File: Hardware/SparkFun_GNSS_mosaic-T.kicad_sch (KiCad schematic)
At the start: 52 parts, among them J2 microSD, SW1 DPDT_Slide_SMD_7.2x3.5mm, SW2 SMD_5.2x5.2mm_h2.5mm, U1 mosaic-T, U4 74LVC2T45DC

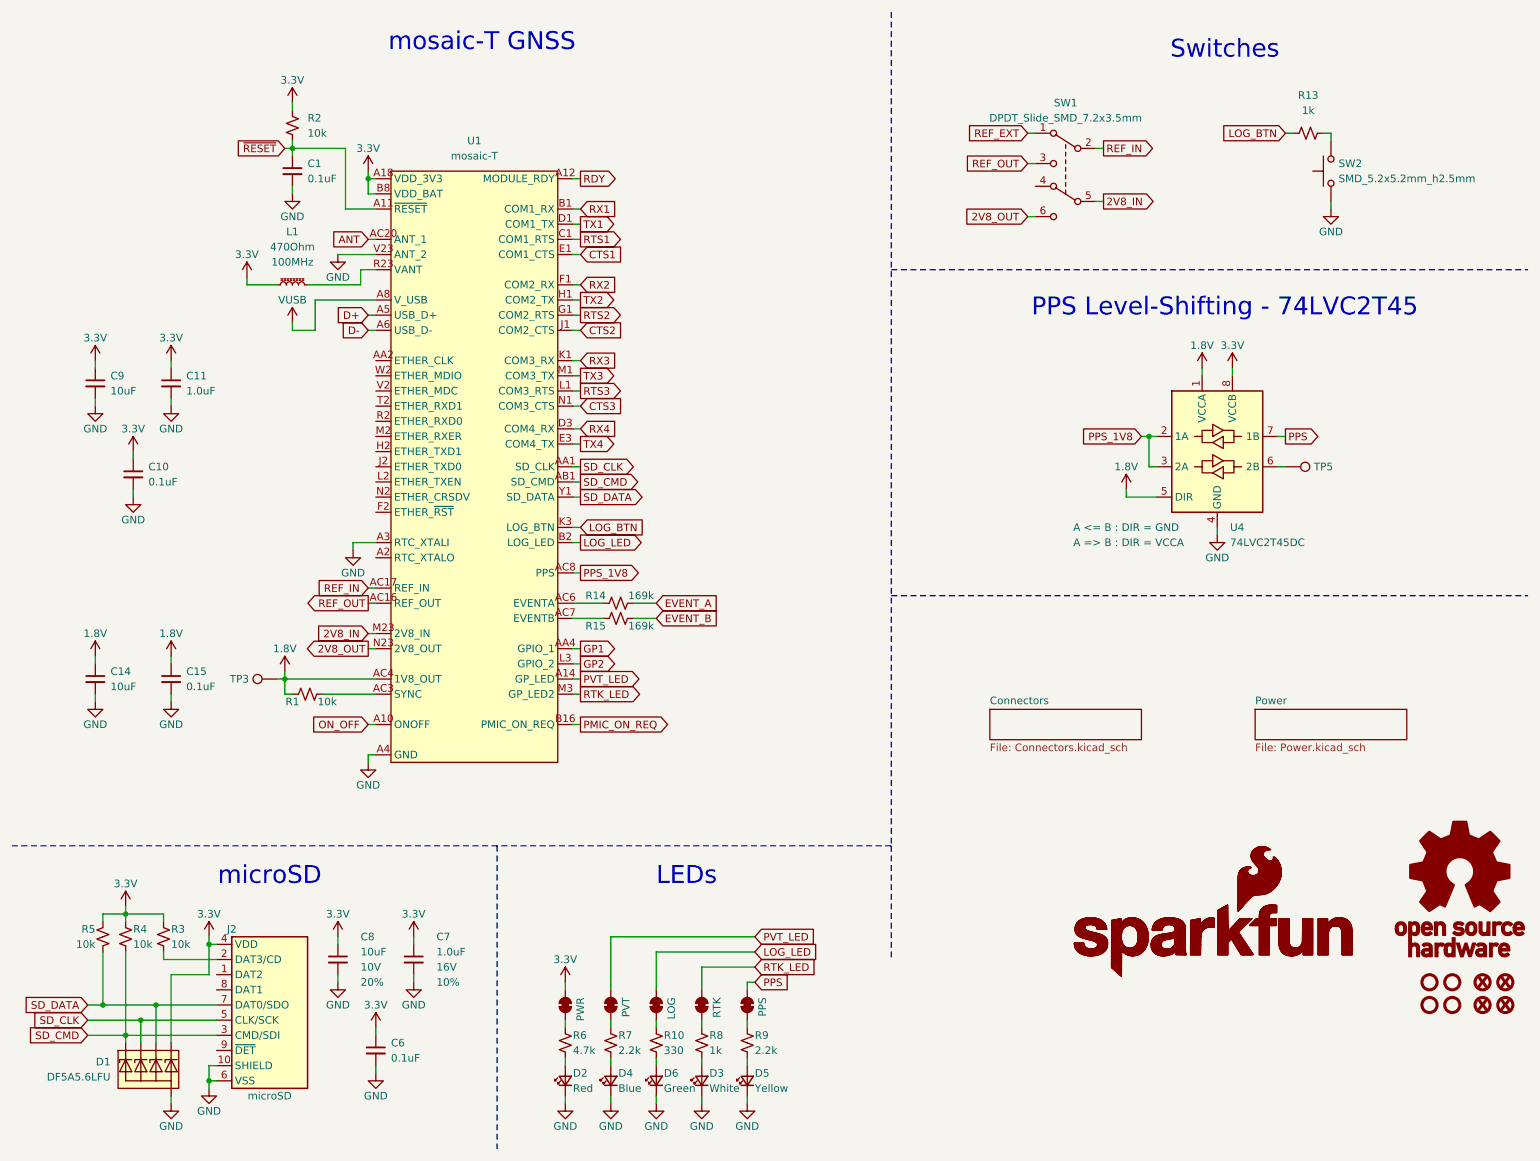
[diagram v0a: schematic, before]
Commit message: Ready for airwire review
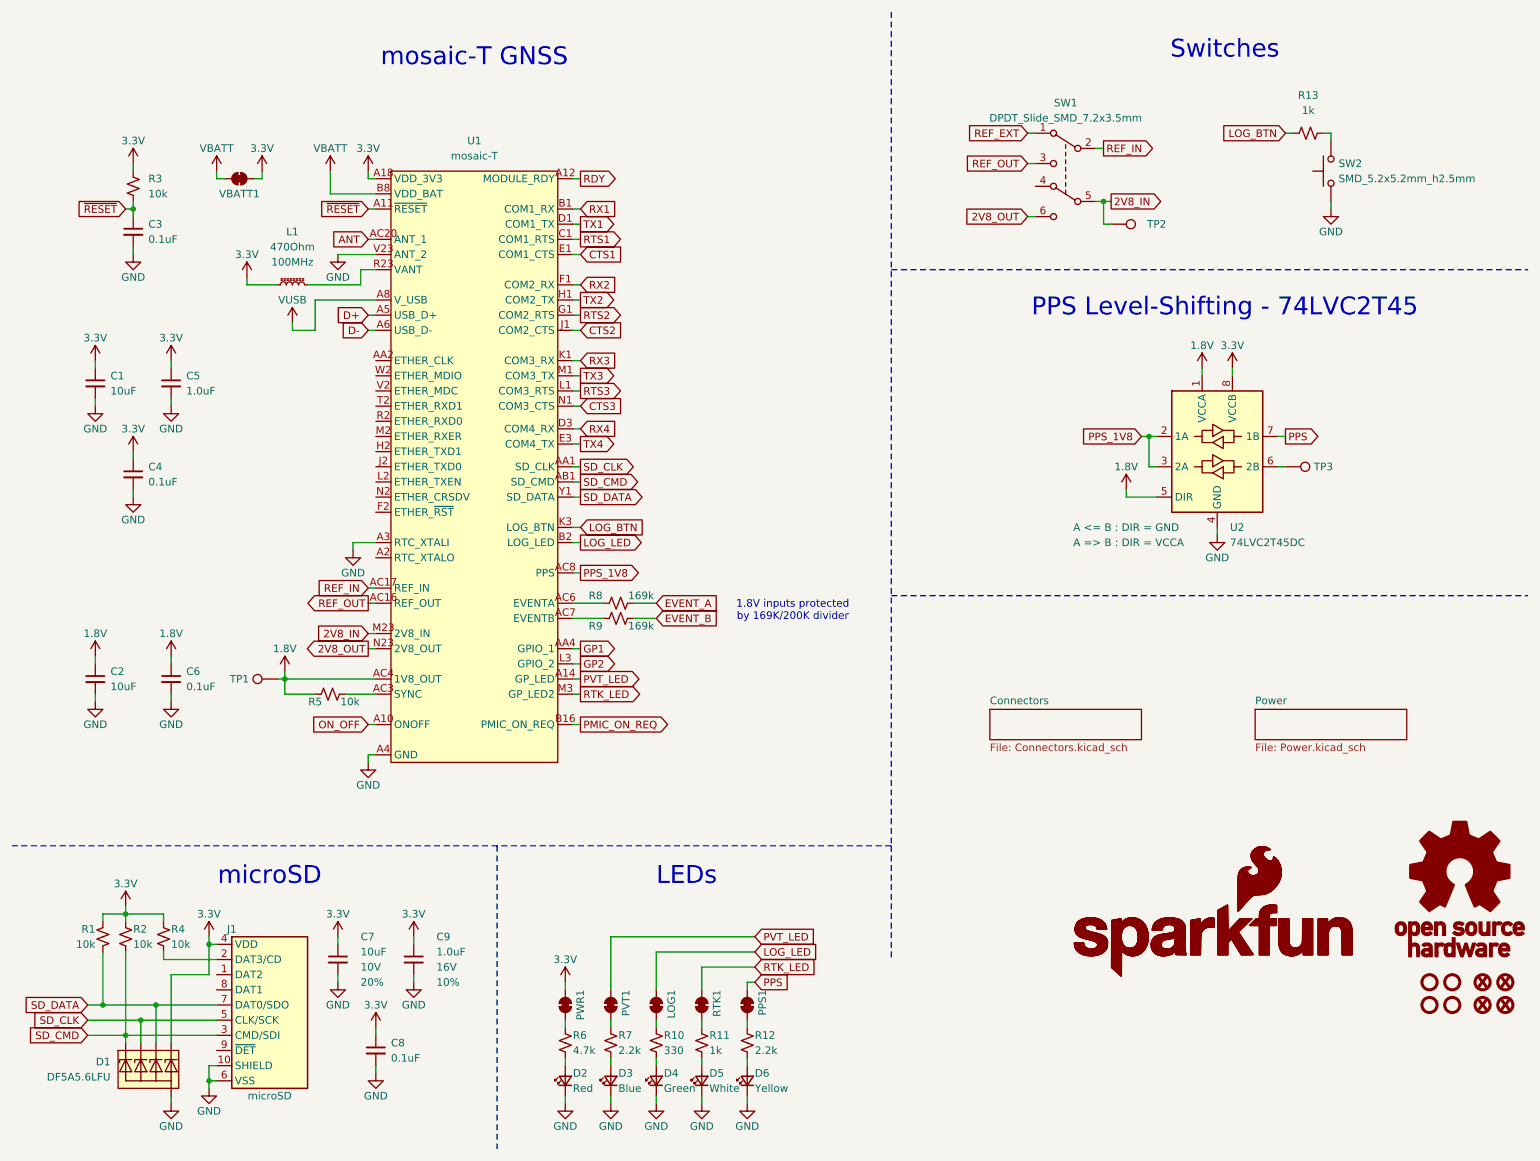
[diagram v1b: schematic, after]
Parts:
- added TP2: 1.25mm, SparkFun-Connector:TestPoint-1.25mm, symbol SparkFun-Connector:TestPoint_1.25mm
- added VBATT1: ~, SparkFun-Jumper:Jumper_2_NC_Trace, symbol SparkFun-Jumper:SolderJumper_2_Bridged
- G1: footprint SparkFun-Aesthetic:SparkFun_Logo_8mm -> (none)
- ST1, ST2, ST3, ST4: value Stand_off -> Standoff
- renumbered C9 to C1, C14 to C2, C1 to C3, C10 to C4, C11 to C5, C15 to C6, C8 to C7, C6 to C8, C7 to C9, D4 to D3, D6 to D4, D3 to D5, D5 to D6, J2 to J1, LOG to LOG1, PPS to PPS1, PVT to PVT1, PWR to PWR1, R5 to R1, R8 to R11, R9 to R12, R4 to R2, R2 to R3, R3 to R4, R1 to R5, R14 to R8, R15 to R9, RTK to RTK1, TP3 to TP1, TP5 to TP3, U4 to U2
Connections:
- net 2V8_IN: now also TP2.1
- net 3.3V: now also VBATT1.1 (A); no longer U1.B8 (VDD_BAT)
- new net VBATT: U1.B8 (VDD_BAT), VBATT1.2 (B)
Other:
- note added: "1.8V inputs protected by 169K/200K divider"
- moved on the sheet: C3, R3, R5

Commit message: Routing - WIP
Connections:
- net 3.3V: now also D1.3 (K2); no longer D1.5 (K4)
- net SD_CLK: now also D1.1 (K1); no longer D1.3 (K2)
- net SD_CMD: now also D1.4 (K3); no longer D1.1 (K1)
- net SD_DATA: now also D1.5 (K4); no longer D1.4 (K3)
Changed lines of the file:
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@@
 	)
 	(junction
-		(at 34.29 181.61)
+		(at 39.37 179.07)
 		(diameter 0)
 		(color 0 0 0 0)
@@
 	)
 	(junction
-		(at 36.83 179.07)
-		(diameter 0)
-		(color 0 0 0 0)
-	)
-	(junction
 		(at 33.02 45.72)
 		(diameter 0)
@@
 	)
 	(junction
+		(at 36.83 184.15)
+		(diameter 0)
+		(color 0 0 0 0)
+	)
+	(junction
 		(at 45.72 168.91)
+		(diameter 0)
+		(color 0 0 0 0)
+	)
+	(junction
+		(at 31.75 181.61)
 		(diameter 0)
 		(color 0 0 0 0)
@@
 	)
 	(junction
-		(at 31.75 184.15)
+		(at 29.21 184.15)
 		(diameter 0)
 		(color 0 0 0 0)
@@
 	(wire
 		(pts
+			(xy 36.83 184.15) (xy 46.99 184.15)
+		)
+		(stroke
+			(width 0)
+			(type default)
+		)
+	)
+	(wire
+		(pts
 			(xy 106.68 45.72) (xy 107.95 45.72)
 		)
@@
 		(pts
 			(xy 46.99 171.45) (xy 38.1 171.45)
+		)
+		(stroke
+			(width 0)
+			(type default)
+		)
+	)
+	(wire
+		(pts
+			(xy 31.75 170.18) (xy 31.75 173.99)
 		)
 		(stroke
@@
 	(wire
 		(pts
-			(xy 34.29 181.61) (xy 34.29 185.42)
-		)
-		(stroke
-			(width 0)
-			(type default)
-		)
-	)
-	(wire
-		(pts
-			(xy 31.75 184.15) (xy 31.75 185.42)
-		)
-		(stroke
-			(width 0)
-			(type default)
-		)
-	)
-	(wire
-		(pts
 			(xy 203.2 83.82) (xy 204.47 83.82)
 		)
@@
 	(wire
 		(pts
+			(xy 31.75 173.99) (xy 29.21 173.99)
+		)
+		(stroke
+			(width 0)
+			(type default)
+		)
+	)
+	(wire
+		(pts
+			(xy 34.29 173.99) (xy 45.72 173.99)
+		)
+		(stroke
+			(width 0)
+			(type default)
+		)
+	)
+	(wire
+		(pts
 			(xy 25.4 179.07) (xy 27.94 179.07)
 		)
@@
 	(wire
 		(pts
+			(xy 29.21 184.15) (xy 36.83 184.15)
+		)
+		(stroke
+			(width 0)
+			(type default)
+		)
+	)
+	(wire
+		(pts
 			(xy 196.85 48.26) (xy 195.58 48.26)
 		)
@@
 	(wire
 		(pts
+			(xy 36.83 184.15) (xy 36.83 185.42)
+		)
+		(stroke
+			(width 0)
+			(type default)
+		)
+	)
+	(wire
+		(pts
 			(xy 59.69 64.77) (xy 59.69 66.04)
 		)
@@
 	(wire
 		(pts
-			(xy 31.75 184.15) (xy 46.99 184.15)
+			(xy 25.4 184.15) (xy 29.21 184.15)
 		)
 		(stroke
@@
 	(wire
 		(pts
+			(xy 39.37 179.07) (xy 46.99 179.07)
+		)
+		(stroke
+			(width 0)
+			(type default)
+		)
+	)
+	(wire
+		(pts
 			(xy 62.23 58.42) (xy 71.12 58.42)
 		)
@@
 	(wire
 		(pts
-			(xy 36.83 179.07) (xy 36.83 185.42)
-		)
-		(stroke
-			(width 0)
-			(type default)
-		)
-	)
-	(wire
-		(pts
 			(xy 106.68 85.09) (xy 107.95 85.09)
 		)
@@
 	(wire
 		(pts
+			(xy 31.75 181.61) (xy 31.75 185.42)
+		)
+		(stroke
+			(width 0)
+			(type default)
+		)
+	)
+	(wire
+		(pts
 			(xy 106.68 48.26) (xy 107.95 48.26)
 		)
@@
 	(wire
 		(pts
-			(xy 39.37 185.42) (xy 39.37 173.99)
-		)
-		(stroke
-			(width 0)
-			(type default)
-		)
-	)
-	(wire
-		(pts
 			(xy 54.61 39.37) (xy 54.61 40.64)
 		)
@@
 	(wire
 		(pts
-			(xy 25.4 181.61) (xy 34.29 181.61)
+			(xy 25.4 181.61) (xy 31.75 181.61)
 		)
 		(stroke
@@
 	(wire
 		(pts
-			(xy 39.37 173.99) (xy 45.72 173.99)
-		)
-		(stroke
-			(width 0)
-			(type default)
-		)
-	)
-	(wire
-		(pts
 			(xy 106.68 73.66) (xy 107.95 73.66)
 		)
@@
 	(wire
 		(pts
-			(xy 31.75 170.18) (xy 31.75 184.15)
-		)
-		(stroke
-			(width 0)
-			(type default)
-		)
-	)
-	(wire
-		(pts
 			(xy 72.39 39.37) (xy 72.39 40.64)
 		)
@@
 	(wire
 		(pts
-			(xy 34.29 181.61) (xy 46.99 181.61)
-		)
-		(stroke
-			(width 0)
-			(type default)
-		)
-	)
-	(wire
-		(pts
 			(xy 27.94 170.18) (xy 27.94 179.07)
 		)
@@
 	(wire
 		(pts
-			(xy 25.4 184.15) (xy 31.75 184.15)
-		)
-		(stroke
-			(width 0)
-			(type default)
-		)
-	)
-	(wire
-		(pts
 			(xy 46.99 40.64) (xy 48.26 40.64)
 		)
@@
 	(wire
 		(pts
-			(xy 27.94 179.07) (xy 36.83 179.07)
-		)
-		(stroke
-			(width 0)
-			(type default)
-		)
-	)
-	(wire
-		(pts
 			(xy 226.06 33.02) (xy 227.33 33.02)
 		)
@@
 		(pts
 			(xy 224.79 83.82) (xy 226.06 83.82)
+		)
+		(stroke
+			(width 0)
+			(type default)
+		)
+	)
+	(wire
+		(pts
+			(xy 29.21 173.99) (xy 29.21 184.15)
+		)
+		(stroke
+			(width 0)
+			(type default)
+		)
+	)
+	(wire
+		(pts
+			(xy 31.75 181.61) (xy 46.99 181.61)
 		)
 		(stroke
@@
 	(wire
 		(pts
+			(xy 39.37 179.07) (xy 39.37 185.42)
+		)
+		(stroke
+			(width 0)
+			(type default)
+		)
+	)
+	(wire
+		(pts
 			(xy 31.75 45.72) (xy 33.02 45.72)
 		)
@@
 	(wire
 		(pts
+			(xy 34.29 185.42) (xy 34.29 173.99)
+		)
+		(stroke
+			(width 0)
+			(type default)
+		)
+	)
+	(wire
+		(pts
 			(xy 106.68 99.06) (xy 107.95 99.06)
 		)
@@
 	(wire
 		(pts
-			(xy 36.83 179.07) (xy 46.99 179.07)
-		)
-		(stroke
+			(xy 27.94 179.07) (xy 39.37 179.07)
+		)
+		(stroke

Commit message: Routed
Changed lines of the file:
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@@
 	(title_block
 		(title "SparkFun GNSS mosaic-T")
-		(date "2025-03-10")
+		(date "2025-03-13")
 		(rev "v01")
 		(company "SparkFun")
@@
 		(dnp no)
 		(property "Reference" "SW1"
-			(at 189.23 27.94 0)
+			(at 189.23 26.67 0)
 			(effects
 				(font
@@
 		)
 		(property "Value" "DPDT_Slide_SMD_7.2x3.5mm"
-			(at 189.23 30.48 0)
+			(at 189.23 29.21 0)
 			(effects
 				(font
